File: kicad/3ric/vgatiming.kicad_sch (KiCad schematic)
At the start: 5 parts, among them U3 74LS574

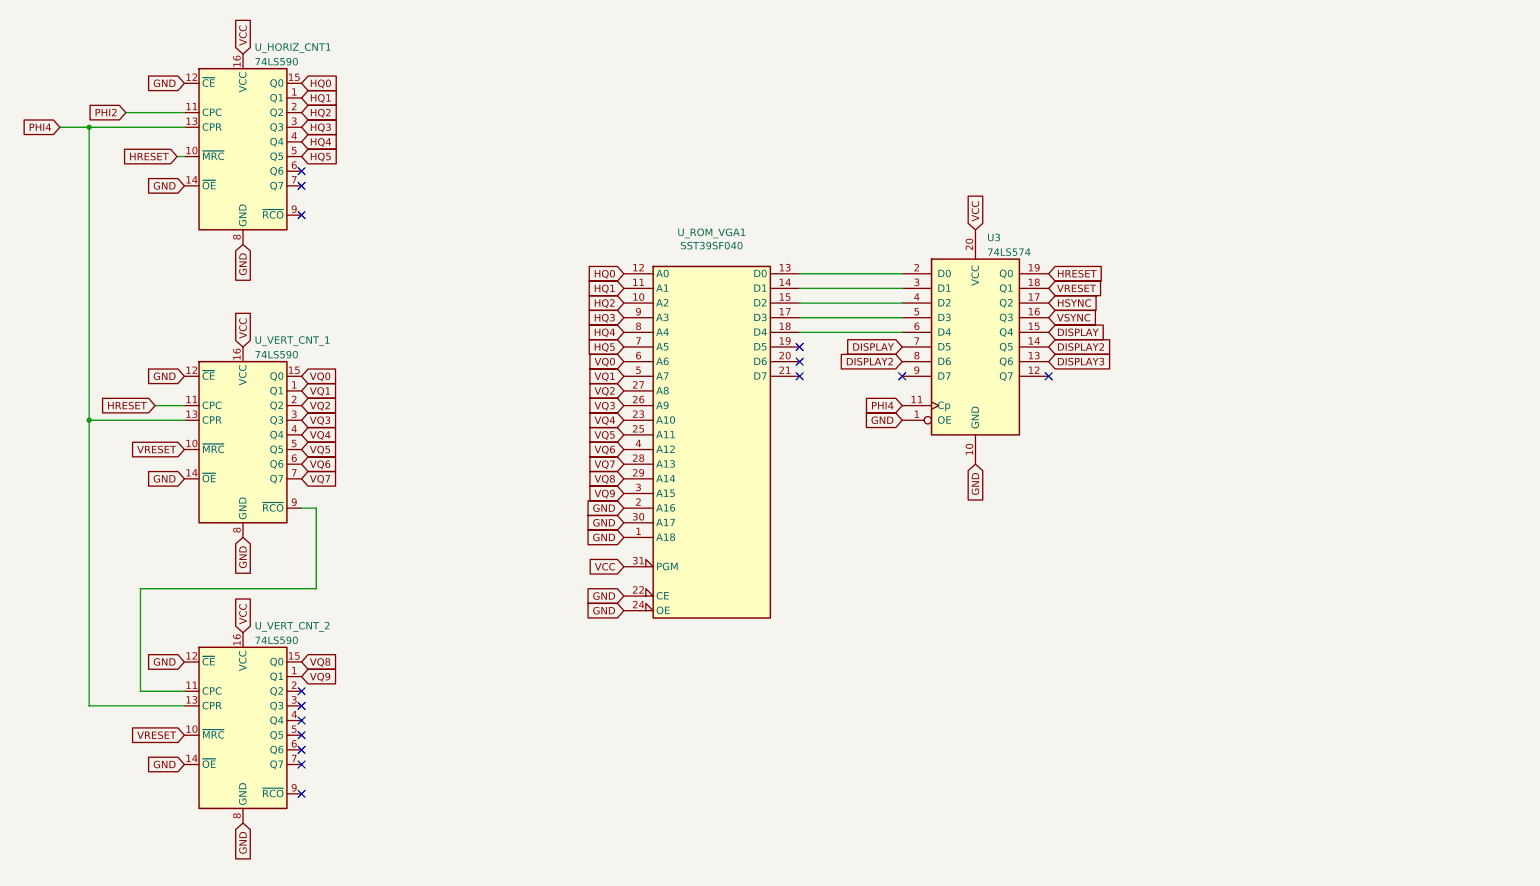
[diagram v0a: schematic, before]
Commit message: schematic updates - bring the schematics up to match breadboard changes current state has high res Apple II color emulation working
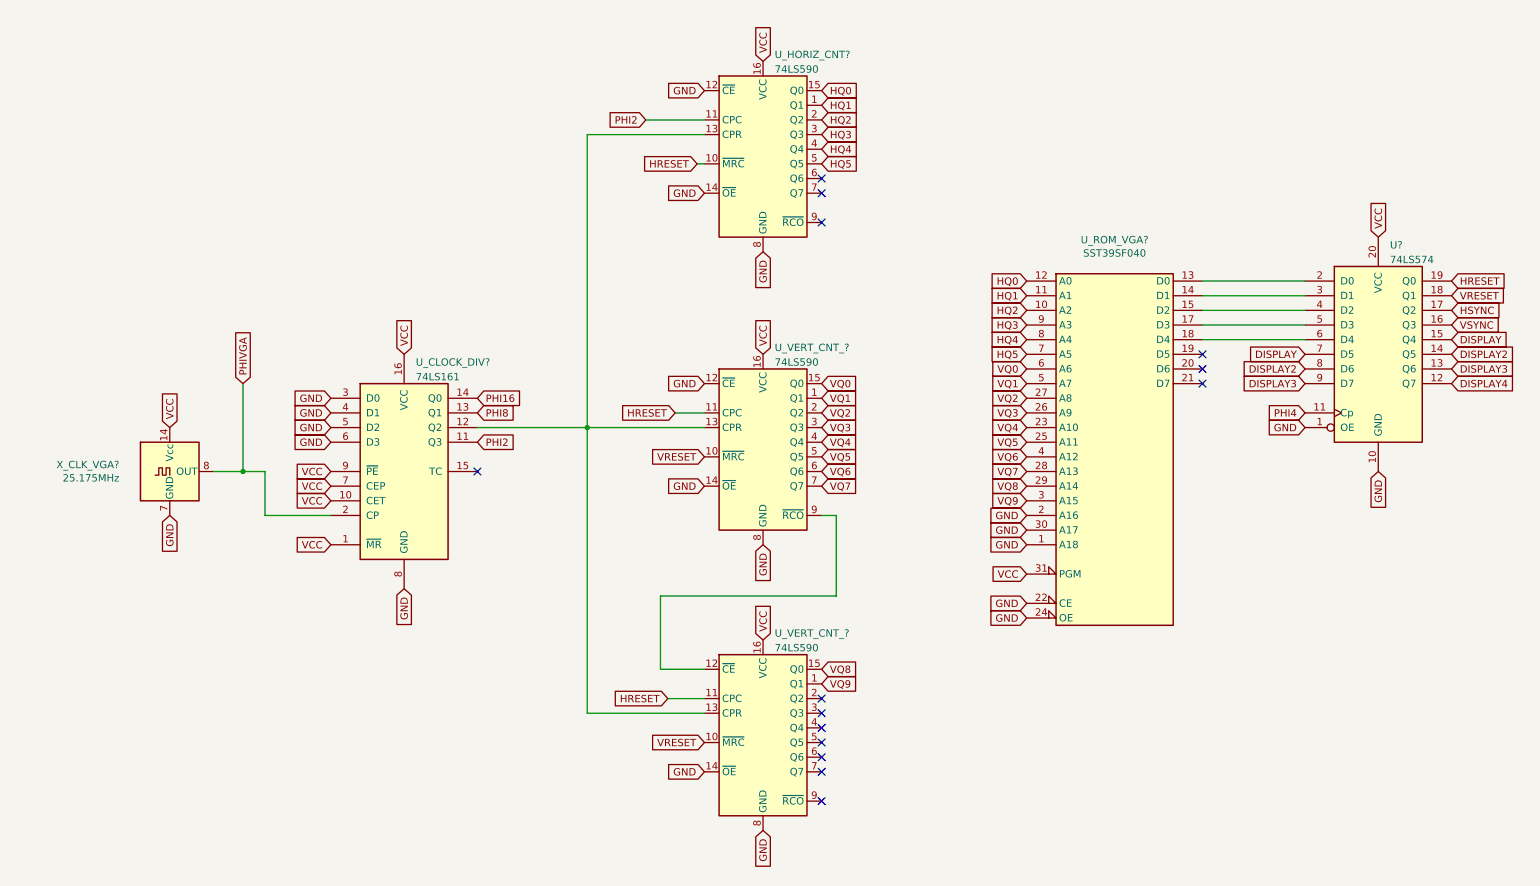
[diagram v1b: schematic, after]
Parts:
- added U_CLOCK_DIV?: 74LS161, Package_DIP:DIP-16_W7.62mm_Socket, symbol 74xx:74LS161
- added X_CLK_VGA?: 25.175MHz, Oscillator:Oscillator_DIP-14, symbol Oscillator:ACO-xxxMHz
- renumbered U3 to U?, U_HORIZ_CNT1 to U_HORIZ_CNT?, U_ROM_VGA1 to U_ROM_VGA?, U_VERT_CNT_2 to U_VERT_CNT_?, U_VERT_CNT_1 to U_VERT_CNT_?
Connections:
- net DISPLAY3: now also U?.9 (D7)
- net GND: now also U_CLOCK_DIV?.3 (D0), U_CLOCK_DIV?.4 (D1), U_CLOCK_DIV?.5 (D2), U_CLOCK_DIV?.6 (D3), U_CLOCK_DIV?.8 (GND), X_CLK_VGA?.7 (GND); no longer U_VERT_CNT_?.12 (~{CE})
- net HRESET: now also U_VERT_CNT_?.11 (CPC)
- net PHI2: now also U_CLOCK_DIV?.11 (Q3)
- net PHI4: no longer U_HORIZ_CNT?.13 (CPR), U_VERT_CNT_?.13 (CPR), U_VERT_CNT_?.13 (CPR)
- net VCC: now also U_CLOCK_DIV?.1 (~{MR}), U_CLOCK_DIV?.10 (CET), U_CLOCK_DIV?.16 (VCC), U_CLOCK_DIV?.7 (CEP), U_CLOCK_DIV?.9 (~{PE}), X_CLK_VGA?.14 (Vcc)
- net at U_VERT_CNT_?.9 (~{RCO}): now also U_VERT_CNT_?.12 (~{CE}); no longer U_VERT_CNT_?.11 (CPC)
- net DISPLAY4: now reaches U?.12 (Q7)
- new net: U_CLOCK_DIV?.12 (Q2), U_HORIZ_CNT?.13 (CPR), U_VERT_CNT_?.13 (CPR), U_VERT_CNT_?.13 (CPR)
- new net PHI16: U_CLOCK_DIV?.14 (Q0)
- new net PHI8: U_CLOCK_DIV?.13 (Q1)
- new net PHIVGA: U_CLOCK_DIV?.2 (CP), X_CLK_VGA?.8 (OUT)
- no-connect marks 15 -> 14
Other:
- moved on the sheet: U?, U_HORIZ_CNT?, U_ROM_VGA?, U_VERT_CNT_?

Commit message: update schematics
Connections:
- net GND: now also U_VERT_CNT_?.12 (~{CE})
- net HRESET: no longer U_VERT_CNT_?.11 (CPC)
- net PHI2: now also U_VERT_CNT_?.13 (CPR), U_VERT_CNT_?.13 (CPR)
- net at U_VERT_CNT_?.9 (~{RCO}): now also U_VERT_CNT_?.11 (CPC); no longer U_VERT_CNT_?.12 (~{CE})
- net at U_CLOCK_DIV?.12 (Q2), U_HORIZ_CNT?.13 (CPR): no longer U_VERT_CNT_?.13 (CPR), U_VERT_CNT_?.13 (CPR)
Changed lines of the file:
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@@
 (kicad_sch (version 20211123) (generator eeschema)
   (paper "A4")
-  (junction (at 115.57 99.06) (diameter 0) (color 0 0 0 0)
-  )
   (junction (at 55.88 106.68) (diameter 0) (color 0 0 0 0)
   )
@@
   (no_connect (at 222.25 91.44))
   (no_connect (at 222.25 88.9))
-  (wire (pts (xy 128.27 128.27) (xy 128.27 140.97))
+  (wire (pts (xy 128.27 128.27) (xy 128.27 146.05))
     (stroke (width 0) (type default) (color 0 0 0 0))
   )
@@
     (stroke (width 0) (type default) (color 0 0 0 0))
   )
-  (wire (pts (xy 128.27 140.97) (xy 135.89 140.97))
-    (stroke (width 0) (type default) (color 0 0 0 0))
-  )
   (wire (pts (xy 240.03 73.66) (xy 222.25 73.66))
     (stroke (width 0) (type default) (color 0 0 0 0))
@@
     (stroke (width 0) (type default) (color 0 0 0 0))
   )
-  (wire (pts (xy 115.57 99.06) (xy 135.89 99.06))
-    (stroke (width 0) (type default) (color 0 0 0 0))
-  )
   (wire (pts (xy 115.57 48.26) (xy 115.57 99.06))
     (stroke (width 0) (type default) (color 0 0 0 0))
   )
-  (wire (pts (xy 125.73 45.72) (xy 135.89 45.72))
+  (wire (pts (xy 106.68 45.72) (xy 135.89 45.72))
     (stroke (width 0) (type default) (color 0 0 0 0))
   )
@@
     (stroke (width 0) (type default) (color 0 0 0 0))
   )
-  (wire (pts (xy 115.57 148.59) (xy 135.89 148.59))
-    (stroke (width 0) (type default) (color 0 0 0 0))
-  )
   (wire (pts (xy 240.03 83.82) (xy 222.25 83.82))
     (stroke (width 0) (type default) (color 0 0 0 0))
@@
     (stroke (width 0) (type default) (color 0 0 0 0))
   )
-  (wire (pts (xy 129.54 146.05) (xy 135.89 146.05))
-    (stroke (width 0) (type default) (color 0 0 0 0))
-  )
-  (wire (pts (xy 115.57 99.06) (xy 115.57 148.59))
+  (wire (pts (xy 128.27 146.05) (xy 135.89 146.05))
     (stroke (width 0) (type default) (color 0 0 0 0))
   )
@@
     )
   )
-  (global_label "HRESET" (shape input) (at 129.54 146.05 180) (fields_autoplaced)
-    (effects (font (size 1.27 1.27)) (justify right))
-    (property "Intersheet References" "${INTERSHEET_REFS}" (id 0) (at 120.0512 145.9706 0)
-      (effects (font (size 1.27 1.27)) (justify right) hide)
-    )
-  )
   (global_label "GND" (shape input) (at 252.73 106.68 270) (fields_autoplaced)
     (effects (font (size 1.27 1.27)) (justify right))
@@
     )
   )
-  (global_label "PHI2" (shape input) (at 125.73 45.72 180) (fields_autoplaced)
-    (effects (font (size 1.27 1.27)) (justify right))
-    (property "Intersheet References" "${INTERSHEET_REFS}" (id 0) (at 118.9021 45.6406 0)
+  (global_label "PHI2" (shape input) (at 106.68 45.72 180) (fields_autoplaced)
+    (effects (font (size 1.27 1.27)) (justify right))
+    (property "Intersheet References" "${INTERSHEET_REFS}" (id 0) (at 99.8521 45.6406 0)
       (effects (font (size 1.27 1.27)) (justify right) hide)
     )
@@
     )
   )
+  (global_label "PHI2" (shape input) (at 135.89 148.59 180) (fields_autoplaced)
+    (effects (font (size 1.27 1.27)) (justify right))
+    (property "Intersheet References" "${INTERSHEET_REFS}" (id 0) (at 129.0621 148.5106 0)
+      (effects (font (size 1.27 1.27)) (justify right) hide)
+    )
+  )
   (global_label "DISPLAY4" (shape input) (at 265.43 91.44 0) (fields_autoplaced)
     (effects (font (size 1.27 1.27)) (justify left))
@@
     )
   )
+  (global_label "PHI2" (shape input) (at 135.89 99.06 180) (fields_autoplaced)
+    (effects (font (size 1.27 1.27)) (justify right))
+    (property "Intersheet References" "${INTERSHEET_REFS}" (id 0) (at 129.0621 98.9806 0)
+      (effects (font (size 1.27 1.27)) (justify right) hide)
+    )
+  )
   (global_label "VCC" (shape input) (at 146.05 35.56 90) (fields_autoplaced)
     (effects (font (size 1.27 1.27)) (justify left))
@@
       (effects (font (size 1.27 1.27)) (justify right) hide)
     )
+  )
+  (global_label "GND" (shape input) (at 135.89 140.97 180) (fields_autoplaced)
+    (effects (font (size 1.27 1.27)) (justify right))
+    (property "Intersheet References" "${INTERSHEET_REFS}" (id 0) (at 129.6064 140.8906 0)
+      (effects (font (size 1.27 1.27)) (justify right) hide)
+    )

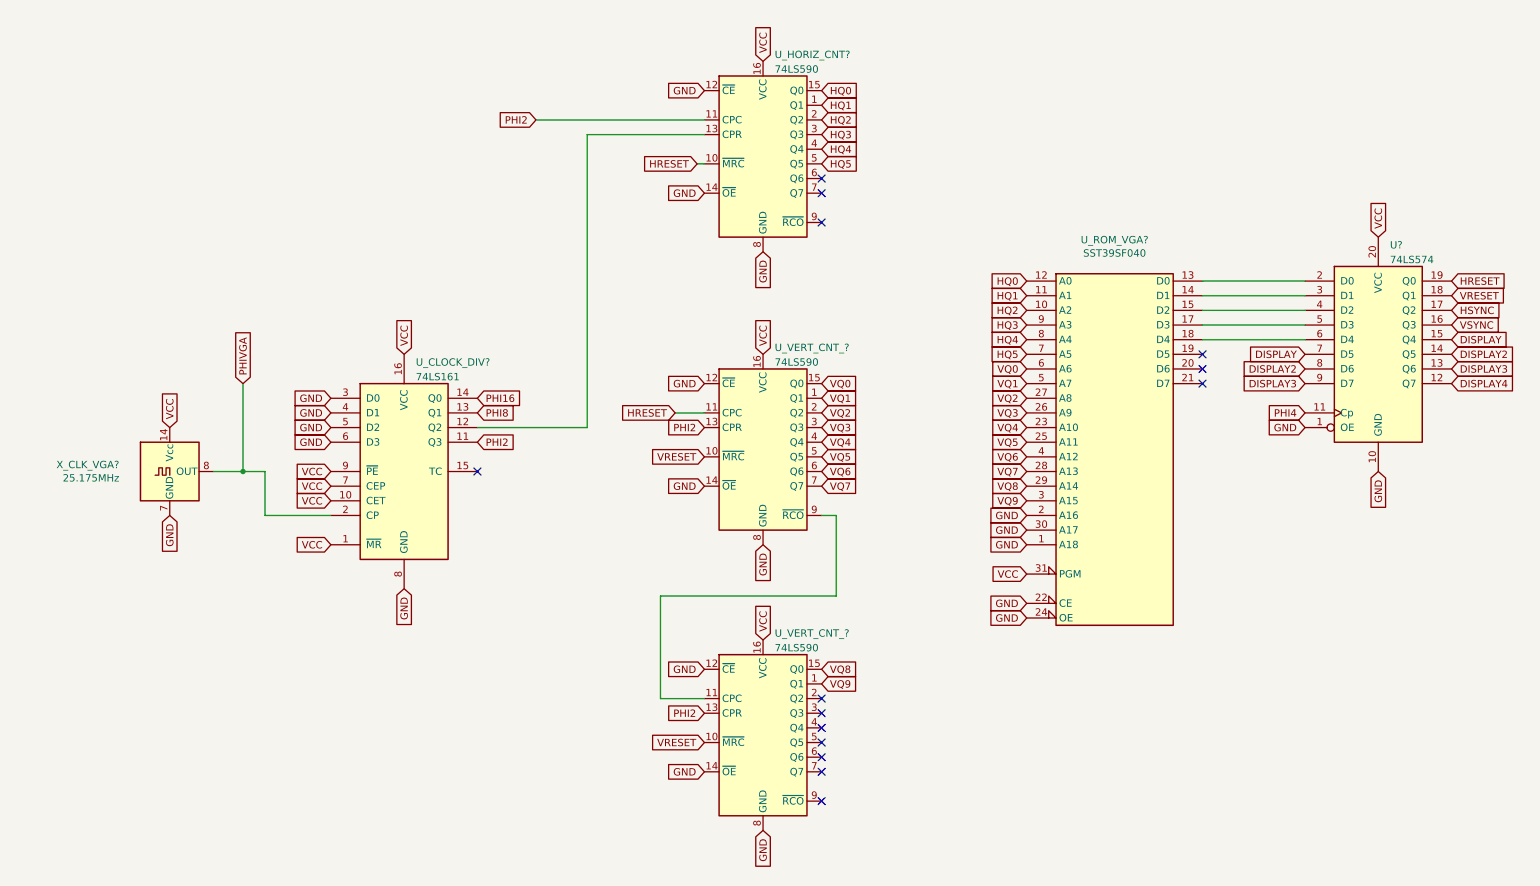
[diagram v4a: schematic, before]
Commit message: update schematic based on breadboard
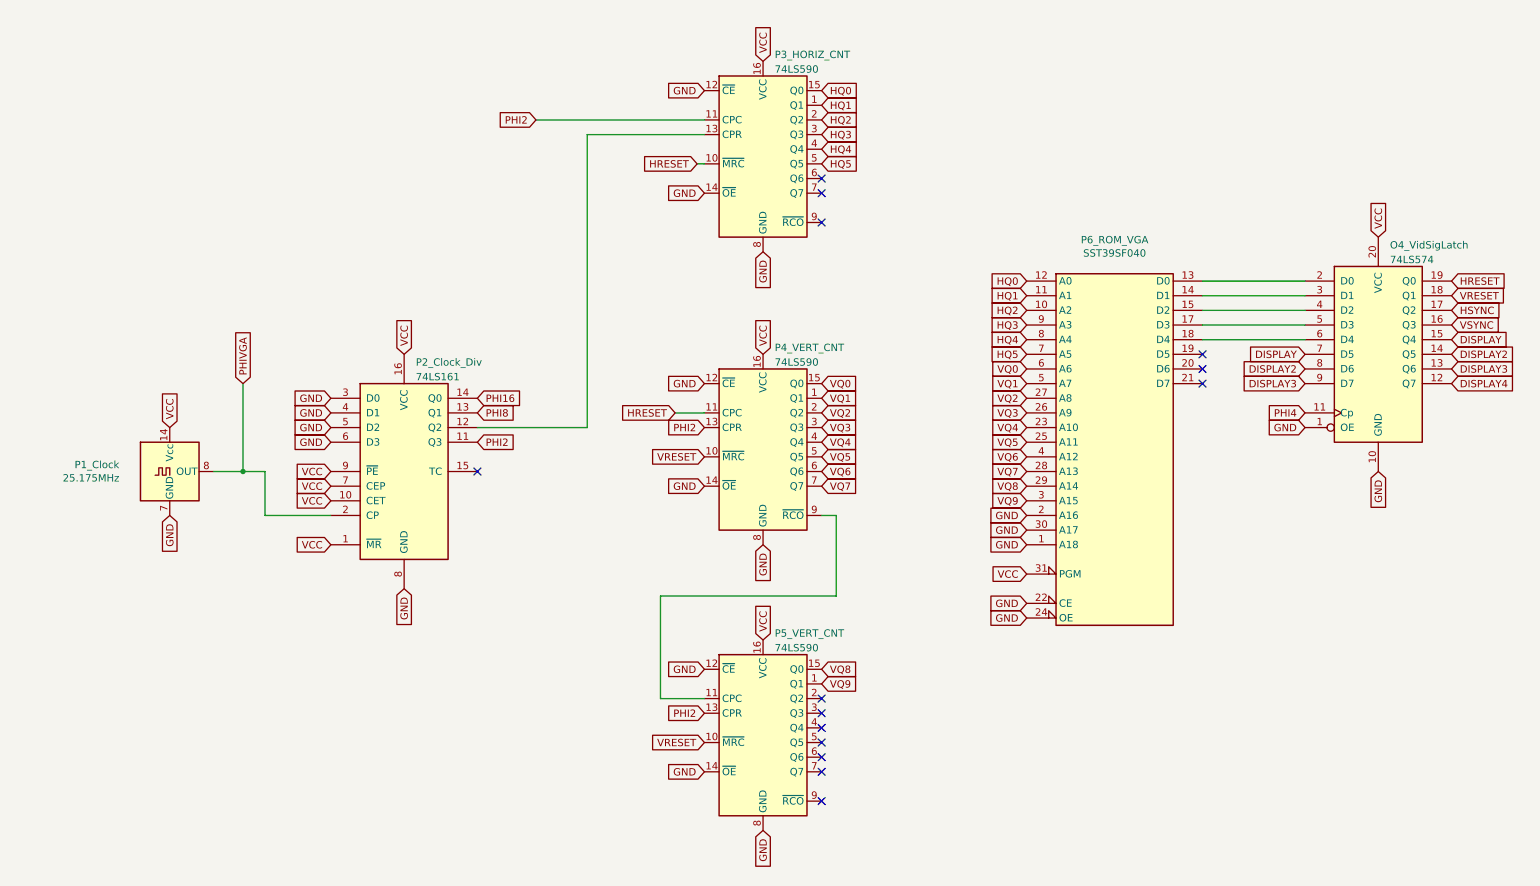
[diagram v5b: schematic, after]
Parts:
- gave numbers to parts that had none: 7
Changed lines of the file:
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@@
 		(dnp no)
 		(fields_autoplaced yes)
-		(property "Reference" "U_VERT_CNT_?"
+		(property "Reference" "P5_VERT_CNT"
 			(at 148.0694 134.7302 0)
 			(effects
@@
 			(project "3ric"
 				(path "/e63e39d7-6ac0-4ffd-8aa3-1841a4541b55/16ecb62b-433c-4b3d-ae08-a168010e2dc7"
-					(reference "U_VERT_CNT_?")
+					(reference "P5_VERT_CNT")
 					(unit 1)
 				)
@@
 		(dnp no)
 		(fields_autoplaced yes)
-		(property "Reference" "U?"
+		(property "Reference" "O4_VidSigLatch"
 			(at 254.7494 67.4202 0)
 			(effects
@@
 			(project "3ric"
 				(path "/e63e39d7-6ac0-4ffd-8aa3-1841a4541b55/16ecb62b-433c-4b3d-ae08-a168010e2dc7"
-					(reference "U?")
+					(reference "O4_VidSigLatch")
 					(unit 1)
 				)
@@
 		(dnp no)
 		(fields_autoplaced yes)
-		(property "Reference" "U_HORIZ_CNT?"
+		(property "Reference" "P3_HORIZ_CNT"
 			(at 148.0694 34.4002 0)
 			(effects
@@
 			(project "3ric"
 				(path "/e63e39d7-6ac0-4ffd-8aa3-1841a4541b55/16ecb62b-433c-4b3d-ae08-a168010e2dc7"
-					(reference "U_HORIZ_CNT?")
+					(reference "P3_HORIZ_CNT")
 					(unit 1)
 				)
@@
 		(dnp no)
 		(fields_autoplaced yes)
-		(property "Reference" "U_VERT_CNT_?"
+		(property "Reference" "P4_VERT_CNT"
 			(at 148.0694 85.2002 0)
 			(effects
@@
 			(project "3ric"
 				(path "/e63e39d7-6ac0-4ffd-8aa3-1841a4541b55/16ecb62b-433c-4b3d-ae08-a168010e2dc7"
-					(reference "U_VERT_CNT_?")
+					(reference "P4_VERT_CNT")
 					(unit 1)
 				)
@@
 		(dnp no)
 		(fields_autoplaced yes)
-		(property "Reference" "U_CLOCK_DIV?"
+		(property "Reference" "P2_Clock_Div"
 			(at 85.8394 87.7402 0)
 			(effects
@@
 			(project "3ric"
 				(path "/e63e39d7-6ac0-4ffd-8aa3-1841a4541b55/16ecb62b-433c-4b3d-ae08-a168010e2dc7"
-					(reference "U_CLOCK_DIV?")
+					(reference "P2_Clock_Div")
 					(unit 1)
 				)
@@
 		(on_board yes)
 		(dnp no)
-		(property "Reference" "U_ROM_VGA?"
+		(property "Reference" "P6_ROM_VGA"
 			(at 207.01 66.5226 0)
 			(effects
@@
 			(project "3ric"
 				(path "/e63e39d7-6ac0-4ffd-8aa3-1841a4541b55/16ecb62b-433c-4b3d-ae08-a168010e2dc7"
-					(reference "U_ROM_VGA?")
+					(reference "P6_ROM_VGA")
 					(unit 1)
 				)
@@
 		(on_board yes)
 		(dnp no)
-		(property "Reference" "X_CLK_VGA?"
+		(property "Reference" "P1_Clock"
 			(at 34.4424 105.5116 0)
 			(effects
@@
 			(project "3ric"
 				(path "/e63e39d7-6ac0-4ffd-8aa3-1841a4541b55/16ecb62b-433c-4b3d-ae08-a168010e2dc7"
-					(reference "X_CLK_VGA?")
+					(reference "P1_Clock")
 					(unit 1)
 				)
